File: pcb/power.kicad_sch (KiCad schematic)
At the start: 32 parts, among them Q201 IRL540N, T201 DA2032-AL, U201 LM5155

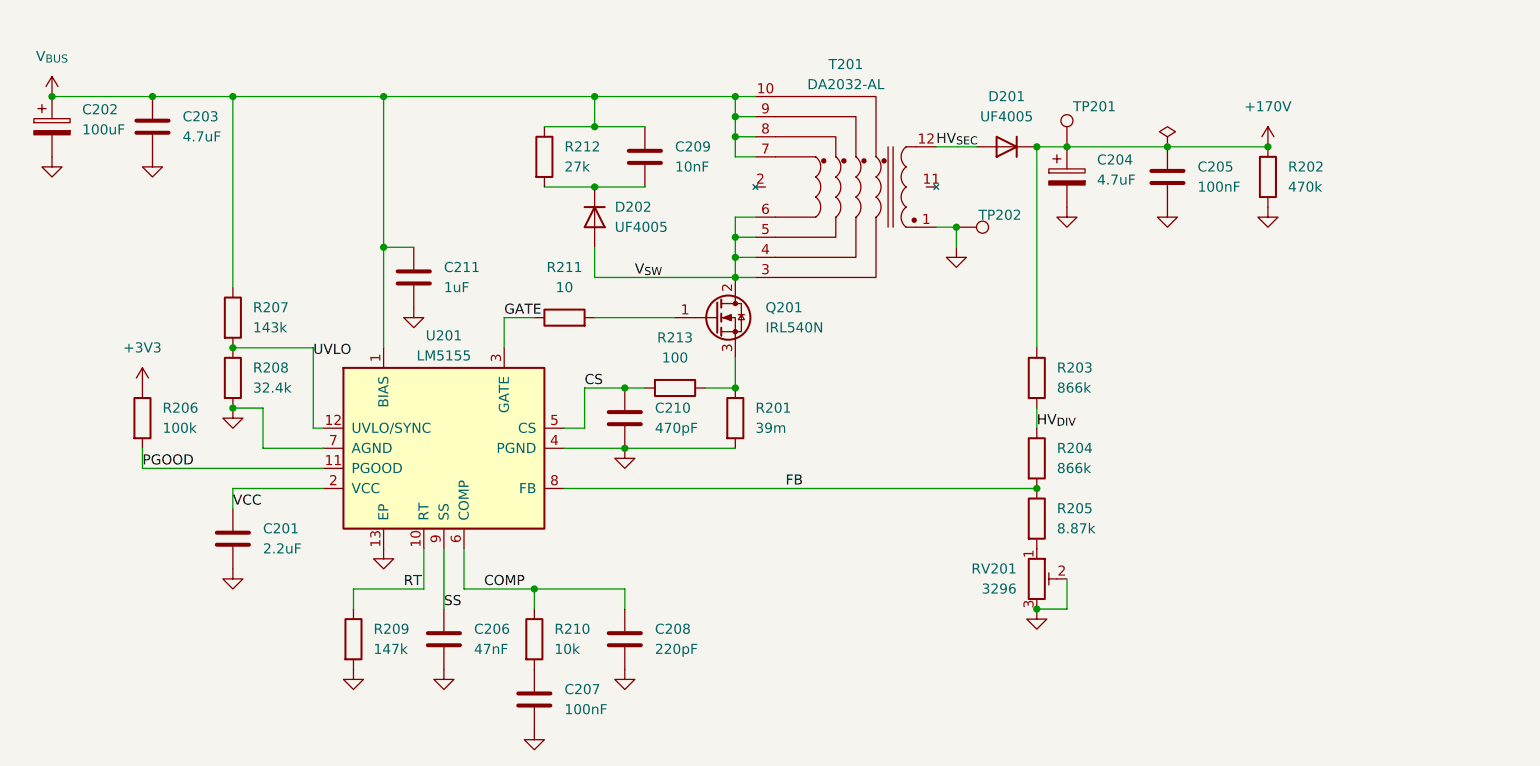
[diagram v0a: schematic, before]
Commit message: Add USB-PD and 3.3V and 5v converters
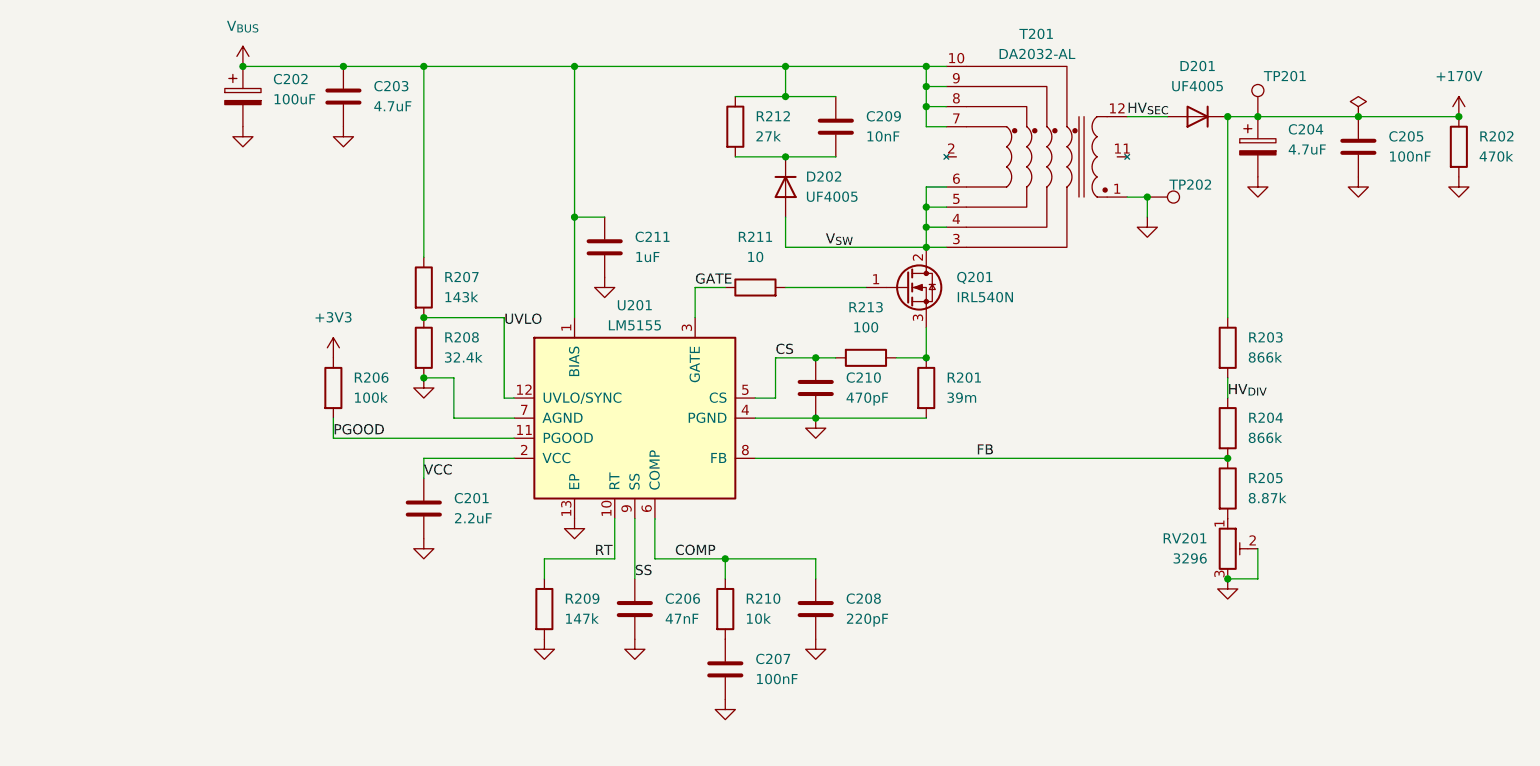
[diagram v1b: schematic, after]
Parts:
- TP201: value TestPoint -> +170V
- TP202: value TestPoint -> GND
- U201: footprint nixie_clock:WSON-12-1EP_3x2mm_P0.5mm_EP1x2.65_ThermalVias -> Package_SON:WSON-12-1EP_3x2mm_P0.5mm_EP1x2.65_ThermalVias
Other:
- moved on the sheet: C201, C202, C203, C204, C205, C206, C207, C208, C209, C210, C211, D201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
